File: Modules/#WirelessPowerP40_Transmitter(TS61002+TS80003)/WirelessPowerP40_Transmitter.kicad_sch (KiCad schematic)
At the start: 133 parts, among them J1 USBA, J2 I2C, J3 I2C, J4 Coil Therm, J5 COIL 20uH, J6 Conn_01x02_Male, J7 Conn_01x02_Male, U1 TS30041, U2 TS94033, U3 74LVC1G66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

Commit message: add PD(19V3A) support for WirelessPowerP40_Transmitter
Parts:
- added U10: HUSB238, Package_DFN_QFN:DFN-10-1EP_3x3mm_P0.5mm_EP1.65x2.38mm, symbol Hynetek:HUSB238
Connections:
- net GND: now also U10.11 (GND)
- net HT: now also U10.1 (VIN)
- net D-: now reaches J1.2 (D-)
- net D-: now also U10.3 (D-)
- net D+: now reaches J1.3 (D+)
- net D+: now also U10.2 (D+)
- net CC: now reaches J1.5 (F)
- net CC: now also U10.4 (CC1)
- no-connect marks 16 -> 19
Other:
- moved on the sheet: C25, C28, C31, C32, C35, C36, C37, C38, C39, C40, C41, C43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

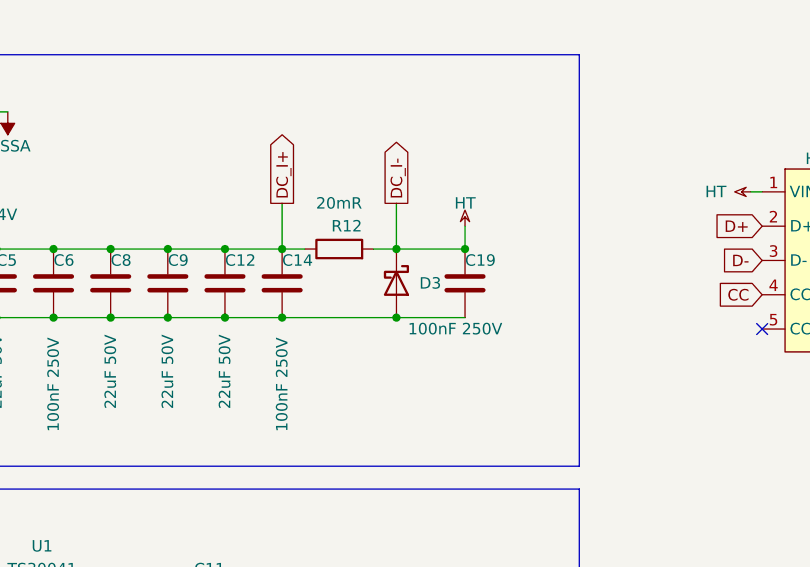
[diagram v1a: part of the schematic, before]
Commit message: WirelessPowerP40_Transmitter > change D3 value with pacific diode
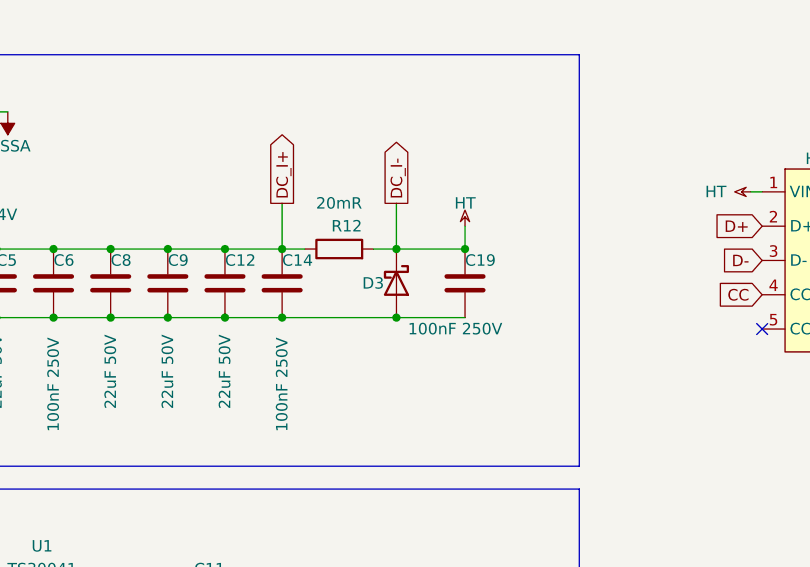
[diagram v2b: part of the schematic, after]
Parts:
- D3: value 28V -> BZT52C30 30V
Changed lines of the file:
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@@
   (symbol (lib_id "Device:D_Schottky") (at 99.06 46.99 270) (unit 1)
     (in_bom yes) (on_board yes)
-    (property "Reference" "D3" (id 0) (at 101.6 46.99 90)
-      (effects (font (size 1.27 1.27)) (justify left))
-    )
-    (property "Value" "28V" (id 1) (at 101.092 48.8566 90)
+    (property "Reference" "D3" (id 0) (at 95.25 46.99 90)
+      (effects (font (size 1.27 1.27)) (justify left))
+    )
+    (property "Value" "BZT52C30 30V" (id 1) (at 101.092 48.8566 90)
       (effects (font (size 1.27 1.27)) (justify left) hide)
     )
@@
     )
     (path "/33df2fad-6122-421c-9eda-5253d481cf10"
-      (reference "D3") (unit 1) (value "28V") (footprint "Diode_SMD:D_0805_2012Metric")
+      (reference "D3") (unit 1) (value "BZT52C30 30V") (footprint "Diode_SMD:D_0805_2012Metric")
     )
     (path "/955631f0-539a-4575-ac32-cb56699bab8b"

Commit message: update bom
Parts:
- C55: value 4.7uF -> 4.7uF 25V
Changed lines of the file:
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@@
       (effects (font (size 1.27 1.27)) (justify left))
     )
-    (property "Value" "4.7uF" (id 1) (at 314.96 203.2 0)
+    (property "Value" "4.7uF 25V" (id 1) (at 309.88 200.66 0)
       (effects (font (size 1.27 1.27)) (justify left))
     )
@@
     )
     (path "/67a77455-62e1-42e1-8969-ac1bfb352062"
-      (reference "C55") (unit 1) (value "4.7uF") (footprint "Capacitor_SMD:C_0402_1005Metric")
+      (reference "C55") (unit 1) (value "4.7uF 25V") (footprint "Capacitor_SMD:C_0402_1005Metric")
     )
     (path "/851c2200-ac47-4108-9a1e-8ed5adaa0972"

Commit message: fix footprint of 74lvc
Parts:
- U3: footprint Package_SO:TSOP-5_1.65x3.05mm_P0.95mm -> Package_TO_SOT_SMD:SOT-353_SC-70-5
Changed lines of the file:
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@@
     (property "Reference" "U3" (id 0) (at 120.65 208.28 0))
     (property "Value" "74LVC1G66" (id 1) (at 124.46 210.82 0))
-    (property "Footprint" "Package_SO:TSOP-5_1.65x3.05mm_P0.95mm" (id 2) (at 115.57 214.63 0)
+    (property "Footprint" "Package_TO_SOT_SMD:SOT-353_SC-70-5" (id 2) (at 115.57 214.63 0)
       (effects (font (size 1.27 1.27)) hide)
     )
@@
     )
     (path "/c8643f53-1b98-45e8-b27d-3ee379eeaf5b"
-      (reference "U3") (unit 1) (value "74LVC1G66") (footprint "Package_SO:TSOP-5_1.65x3.05mm_P0.95mm")
+      (reference "U3") (unit 1) (value "74LVC1G66") (footprint "Package_TO_SOT_SMD:SOT-353_SC-70-5")
     )
     (path "/e64d24d3-af22-4b21-be4c-da34f739942d"

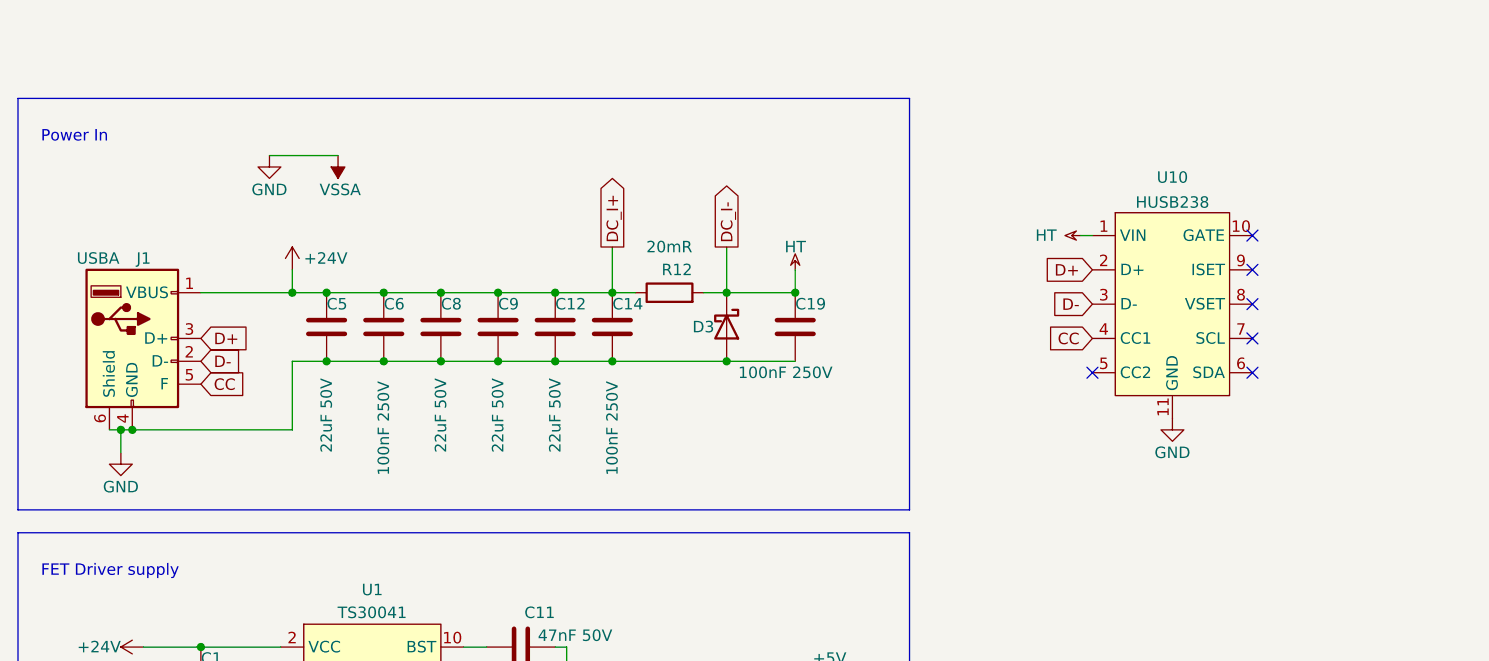
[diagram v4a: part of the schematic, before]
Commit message: replace USB Connector
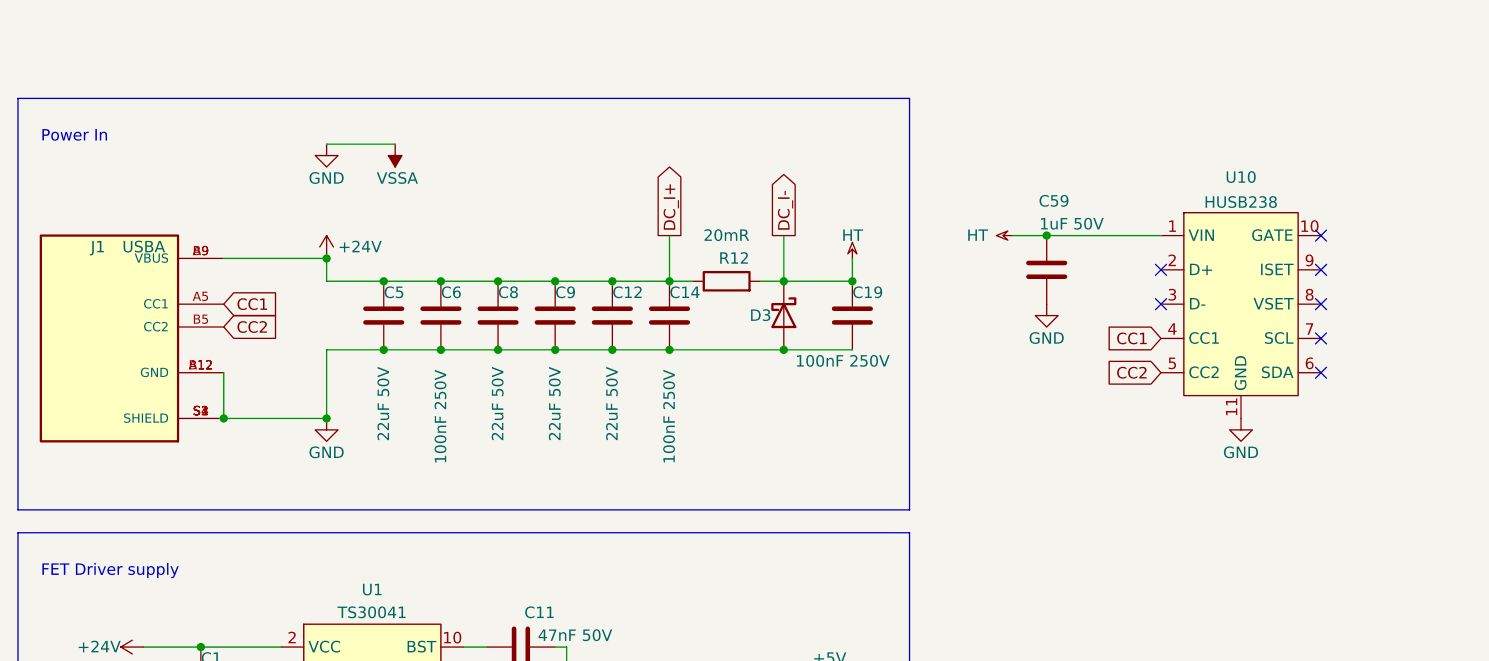
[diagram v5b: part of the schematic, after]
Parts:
- added C59: 1uF 50V, Capacitor_SMD:C_0402_1005Metric, symbol Device:C
- J1: footprint USB_plug:USB_A_2.0_FAST -> USB_plug:USB4125-GF-A_REVA2; symbol USB_Connector:USB_A_F -> USB4125-GF-A_REVA2:USB4125-GF-A_REVA2; MANUFACTURER (none) -> GCT; MAXIMUM_PACKAGE_HEIGHT (none) -> 3.16 mm; PARTREV (none) -> Rev A2; STANDARD (none) -> Manufacturer Recommendations
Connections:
- net +24V: now also J1.A9 (VBUS), J1.B9 (VBUS); no longer J1.1 (VBUS)
- net GND: now also J1.A12 (GND), J1.B12 (GND), J1.S1 (SHIELD), J1.S2 (SHIELD), J1.S3 (SHIELD), J1.S4 (SHIELD), C59.1; no longer J1.4 (GND), J1.6 (Shield)
- net HT: now also C59.2
- net CC2: now reaches U10.5 (CC2)
- net CC2: now also J1.B5 (CC2)
- net CC renamed CC1
- net CC1: now also J1.A5 (CC1); no longer J1.5 (F)
- net D+: no longer names the net of U10.2 (D+)
- net D+: no longer J1.3 (D+)
- net D-: no longer names the net of U10.3 (D-)
- net D-: no longer J1.2 (D-)
- no-connect marks 19 -> 20
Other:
- moved on the sheet: C12, C14, C19, C5, C6, C8, C9, D3, R12, U10

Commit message: update USB-Type-C,with QC support
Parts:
- J1: footprint USB_plug:USB4125-GF-A_REVA2 -> USB_plug:SHENZHEN-CHUANGQIN-TECHNOLOGY_CQ-USB-C16PSMT01; symbol USB4125-GF-A_REVA2:USB4125-GF-A_REVA2 -> CQ-USB-C16PSMT01:CQ-USB-C16PSMT01; MANUFACTURER GCT -> Shenzhen Chuangpin Science and Technology; MAXIMUM_PACKAGE_HEIGHT 3.16 mm -> 3.36mm; PARTREV Rev A2 -> A
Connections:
- net +24V: now also J1.A4_B9 (VBUS), J1.B4_A9 (VBUS); no longer J1.A9 (VBUS), J1.B9 (VBUS)
- net GND: now also J1.A1_B12 (GND), J1.B1_A12 (GND); no longer J1.A12 (GND), J1.B12 (GND)
- net D+: now reaches U10.2 (D+)
- net D+: now also J1.A6 (DP1), J1.B6 (DP2)
- net D-: now reaches U10.3 (D-)
- net D-: now also J1.A7 (DN1), J1.B7 (DN2)
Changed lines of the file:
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@@
   (junction (at 34.29 214.63) (diameter 0) (color 0 0 0 0))
   (junction (at 40.64 82.55) (diameter 0) (color 0 0 0 0))
-  (junction (at 43.18 57.15) (diameter 0) (color 0 0 0 0))
   (junction (at 46.99 106.68) (diameter 0) (color 0 0 0 0))
+  (junction (at 50.8 57.15) (diameter 0) (color 0 0 0 0))
   (junction (at 53.34 140.97) (diameter 0) (color 0 0 0 0))
   (junction (at 53.34 148.59) (diameter 0) (color 0 0 0 0))
@@
   (junction (at 375.92 85.09) (diameter 0) (color 0 0 0 0))
   (junction (at 388.62 213.36) (diameter 0) (color 0 0 0 0))
+  (no_connect (at 26.67 54.61))
+  (no_connect (at 26.67 57.15))
   (no_connect (at 49.53 104.14))
   (no_connect (at 62.23 257.81))
-  (no_connect (at 147.32 40.64))
-  (no_connect (at 147.32 44.45))
   (no_connect (at 165.1 36.83))
   (no_connect (at 165.1 40.64))
@@
   (no_connect (at 243.84 255.27))
   (no_connect (at 243.84 257.81))
+  (wire (pts (xy 26.67 43.18) (xy 26.67 45.72))
+    (stroke (width 0) (type default) (color 0 0 0 0))
+  )
+  (wire (pts (xy 26.67 48.26) (xy 26.67 50.8))
+    (stroke (width 0) (type default) (color 0 0 0 0))
+  )
   (wire (pts (xy 30.48 214.63) (xy 34.29 214.63))
     (stroke (width 0.5) (type default) (color 255 1 18 1))
@@
     (stroke (width 0) (type default) (color 0 0 0 0))
   )
-  (wire (pts (xy 43.18 39.37) (xy 54.61 39.37))
-    (stroke (width 0) (type default) (color 0 0 0 0))
-  )
-  (wire (pts (xy 43.18 52.07) (xy 43.18 57.15))
-    (stroke (width 0) (type default) (color 0 0 0 0))
-  )
-  (wire (pts (xy 43.18 57.15) (xy 54.61 57.15))
-    (stroke (width 0) (type default) (color 0 0 0 0))
-  )
   (wire (pts (xy 44.45 106.68) (xy 46.99 106.68))
     (stroke (width 0) (type default) (color 0 0 0 0))
@@
     (stroke (width 0) (type default) (color 0 0 0 0))
   )
+  (wire (pts (xy 50.8 39.37) (xy 54.61 39.37))
+    (stroke (width 0) (type default) (color 0 0 0 0))
+  )
+  (wire (pts (xy 50.8 52.07) (xy 50.8 57.15))
+    (stroke (width 0) (type default) (color 0 0 0 0))
+  )
+  (wire (pts (xy 50.8 57.15) (xy 54.61 57.15))
+    (stroke (width 0) (type default) (color 0 0 0 0))
+  )
   (wire (pts (xy 50.8 252.73) (xy 54.61 252.73))
     (stroke (width 0.5) (type default) (color 255 1 18 1))
@@
     (effects (font (size 1.27 1.27)) (justify left bottom))
   )
+  (global_label "CC1" (shape input) (at 26.67 38.1 180) (fields_autoplaced)
+    (effects (font (size 1.27 1.27)) (justify right))
+    (property "Intersheet References" "${INTERSHEET_REFS}" (id 0) (at 20.5074 38.0206 0)
+      (effects (font (size 1.27 1.27)) (justify right) hide)
+    )
+  )
+  (global_label "CC2" (shape input) (at 26.67 40.64 180) (fields_autoplaced)
+    (effects (font (size 1.27 1.27)) (justify right))
+    (property "Intersheet References" "${INTERSHEET_REFS}" (id 0) (at 20.5074 40.5606 0)
+      (effects (font (size 1.27 1.27)) (justify right) hide)
+    )
+  )
+  (global_label "D+" (shape input) (at 26.67 44.45 180) (fields_autoplaced)
+    (effects (font (size 1.27 1.27)) (justify right))
+    (property "Intersheet References" "${INTERSHEET_REFS}" (id 0) (at 21.4145 44.3706 0)
+      (effects (font (size 1.27 1.27)) (justify right) hide)
+    )
+  )
+  (global_label "D-" (shape input) (at 26.67 49.53 180) (fields_autoplaced)
+    (effects (font (size 1.27 1.27)) (justify right))
+    (property "Intersheet References" "${INTERSHEET_REFS}" (id 0) (at 21.4145 49.4506 0)
+      (effects (font (size 1.27 1.27)) (justify right) hide)
+    )
+  )
   (global_label "COIL-" (shape input) (at 30.48 214.63 180) (fields_autoplaced)
     (effects (font (size 1.27 1.27)) (justify right))
@@
     )
   )
-  (global_label "CC1" (shape input) (at 43.18 44.45 0) (fields_autoplaced)
-    (effects (font (size 1.27 1.27)) (justify left))
-    (property "Intersheet References" "${INTERSHEET_REFS}" (id 0) (at 49.3426 44.3706 0)
-      (effects (font (size 1.27 1.27)) (justify left) hide)
-    )
-  )
-  (global_label "CC2" (shape input) (at 43.18 46.99 0) (fields_autoplaced)
-    (effects (font (size 1.27 1.27)) (justify left))
-    (property "Intersheet References" "${INTERSHEET_REFS}" (id 0) (at 49.3426 46.9106 0)
-      (effects (font (size 1.27 1.27)) (justify left) hide)
-    )
-  )
   (global_label "DRV_EN" (shape input) (at 52.07 156.21 180) (fields_autoplaced)
     (effects (font (size 1.27 1.27)) (justify right))
@@
     )
   )
+  (global_label "D+" (shape input) (at 147.32 40.64 180) (fields_autoplaced)
+    (effects (font (size 1.27 1.27)) (justify right))
+    (property "Intersheet References" "${INTERSHEET_REFS}" (id 0) (at 142.0645 40.5606 0)
+      (effects (font (size 1.27 1.27)) (justify right) hide)
+    )
+  )
+  (global_label "D-" (shape input) (at 147.32 44.45 180) (fields_autoplaced)
+    (effects (font (size 1.27 1.27)) (justify right))
+    (property "Intersheet References" "${INTERSHEET_REFS}" (id 0) (at 142.0645 44.3706 0)
+      (effects (font (size 1.27 1.27)) (justify right) hide)
+    )
+  )
   (global_label "CC1" (shape input) (at 147.32 48.26 180) (fields_autoplaced)
     (effects (font (size 1.27 1.27)) (justify right))
@@
     (pin "7")
   )
-  (symbol (lib_id "USB4125-GF-A_REVA2:USB4125-GF-A_REVA2") (at 30.48 46.99 0) (mirror y) (unit 1)
-    (in_bom yes) (on_board yes)
-    (property "Reference" "J1" (id 0) (at 29.21 38.1 0))
-    (property "Value" "USBA" (id 1) (at 34.29 38.1 0))
-    (property "Footprint" "USB_plug:USB4125-GF-A_REVA2" (id 2) (at 30.48 46.99 0)
-      (effects (font (size 1.27 1.27)) (justify left bottom) hide)
-    )
-    (property "Datasheet" " ~" (id 3) (at 30.48 46.99 0)
-      (effects (font (size 1.27 1.27)) (justify left bottom) hide)
-    )
-    (property "MAXIMUM_PACKAGE_HEIGHT" "3.16 mm" (id 4) (at 30.48 46.99 0)
-      (effects (font (size 1.27 1.27)) (justify left bottom) hide)
-    )
-    (property "STANDARD" "Manufacturer Recommendations" (id 5) (at 30.48 46.99 0)
-      (effects (font (size 1.27 1.27)) (justify left bottom) hide)
-    )
-    (property "PARTREV" "Rev A2" (id 6) (at 30.48 46.99 0)
-      (effects (font (size 1.27 1.27)) (justify left bottom) hide)
-    )
-    (property "MANUFACTURER" "GCT" (id 7) (at 30.48 46.99 0)
-      (effects (font (size 1.27 1.27)) (justify left bottom) hide)
-    )
-    (pin "A12")
-    (pin "A5")
-    (pin "A9")
-    (pin "B12")
-    (pin "B5")
-    (pin "B9")
-    (pin "S1")
-    (pin "S2")
-    (pin "S3")
-    (pin "S4")
-  )
   (symbol (lib_id "TS:TS94033") (at 67.31 152.4 0) (unit 1)
     (in_bom yes) (on_board yes) (fields_autoplaced)
@@
     (pin "9")
   )
+  (symbol (lib_id "CQ-USB-C16PSMT01:CQ-USB-C16PSMT01") (at 38.1 45.72 0) (unit 1)
+    (in_bom yes) (on_board yes)
+    (property "Reference" "J1" (id 0) (at 38.1 29.21 0))
+    (property "Value" "USBA" (id 1) (at 38.1 31.75 0))
+    (property "Footprint" "USB_plug:SHENZHEN-CHUANGQIN-TECHNOLOGY_CQ-USB-C16PSMT01" (id 2) (at 38.1 45.72 0)
+      (effects (font (size 1.27 1.27)) (justify left bottom) hide)
+    )
+    (property "Datasheet" " ~" (id 3) (at 38.1 45.72 0)
+      (effects (font (size 1.27 1.27)) (justify left bottom) hide)
+    )
+    (property "MAXIMUM_PACKAGE_HEIGHT" "3.36mm" (id 4) (at 38.1 45.72 0)
+      (effects (font (size 1.27 1.27)) (justify left bottom) hide)
+    )
+    (property "STANDARD" "Manufacturer Recommendations" (id 5) (at 38.1 45.72 0)
+      (effects (font (size 1.27 1.27)) (justify left bottom) hide)
+    )
+    (property "PARTREV" "A" (id 6) (at 38.1 45.72 0)
+      (effects (font (size 1.27 1.27)) (justify left bottom) hide)
+    )
+    (property "MANUFACTURER" "Shenzhen Chuangpin Science and Technology" (id 7) (at 38.1 45.72 0)
+      (effects (font (size 1.27 1.27)) (justify left bottom) hide)
+    )
+    (pin "A1_B12")
+    (pin "A4_B9")
+    (pin "A5")
+    (pin "A6")
+    (pin "A7")
+    (pin "A8")
+    (pin "B1_A12")
+    (pin "B4_A9")
+    (pin "B5")
+    (pin "B6")
+    (pin "B7")
+    (pin "B8")
+    (pin "S1")
+    (pin "S2")
+    (pin "S3")
+    (pin "S4")
+  )
   (symbol (lib_id "TS:TS61002") (at 248.92 85.09 0) (unit 1)
     (in_bom yes) (on_board yes) (fields_autoplaced)
@@
     )
     (path "/aadfb580-07ac-4146-909c-e21612e4a910"
-      (reference "J1") (unit 1) (value "USBA") (footprint "USB_plug:USB4125-GF-A_REVA2")
+      (reference "J1") (unit 1) (value "USBA") (footprint "USB_plug:SHENZHEN-CHUANGQIN-TECHNOLOGY_CQ-USB-C16PSMT01")
     )
     (path "/315aa701-aff7-4924-b211-8b9bbfa38ab3"
